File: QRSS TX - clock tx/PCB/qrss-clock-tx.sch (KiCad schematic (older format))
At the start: 1 part

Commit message: update QRSS TX schematic
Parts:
- removed U?: ATmega328PB-AU, Package_QFP:TQFP-32_7x7mm_P0.8mm, symbol MCU_Microchip_ATmega:ATmega328PB-AU
- added C1, C3, C4, C6, C7, C8: .1u, symbol Device:C
- added C10, C12: 30p, symbol Device:C
- added C11, C9: 10p, symbol Device:C
- added C2, C5: 100p, symbol Device:C
- added D1: POWER, symbol Device:LED
- added D2: VAR1, symbol Device:D_Capacitance
- added D3: VAR2, symbol Device:D_Capacitance
- added D4: STAT, symbol Device:LED
- added FB1: Ferrite_Bead, symbol Device:Ferrite_Bead
- added J1: PWR, symbol Connector:Conn_01x02_Male
- added J2: ICSP, symbol Connector:Conn_01x05_Male
- added J3: Conn_Coaxial, symbol Connector:Conn_Coaxial
- added Q1: MMBT3904, Package_TO_SOT_SMD:SOT-23, symbol Transistor_BJT:MMBT3904
- added R1, R2, R3, R6: 1K, symbol Device:R
- added R4: 100K, symbol Device:R
- added R5: 10K, symbol Device:R
- added U1, U2: LM78M05_TO252, Package_TO_SOT_SMD:TO-252-2, symbol Regulator_Linear:LM78M05_TO252
- added U3: 74HC04, symbol 74xx:74HC04
- added U4: ATtiny2313A-SU, Package_SO:SOIC-20W_7.5x12.8mm_P1.27mm, symbol MCU_Microchip_ATtiny:ATtiny2313A-SU
- added Y1: 10.14MHz, symbol Device:Crystal
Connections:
- new net: R6.1, U4.2 (PD0)
- new net: C12.1, U4.4 (PA1/XTAL2), Y1.1
- new net: C10.1, U4.5 (PA0/XTAL1), Y1.2
- new net: C11.2, C9.2, D2.1 (K), D3.1 (K), R4.1
- new net: C4.1, FB1.2, J1.2 (Pin_2)
- new net: D1.2 (A), R1.1
- new net: C3.1, R1.2, U2.3 (VO), U3.14 (VCC)
- new net: C7.2, R3.1, R4.2
- new net: Q1.1 (B), R2.1
- new net: D4.2 (A), R6.2
- new net: J3.1 (In), U3.10, U3.12, U3.2, U3.4, U3.6, U3.8
- new net: Q1.2 (E), R3.2
- new net CKOUT: U3.1, U3.11, U3.13, U3.3, U3.5, U3.9, U4.6 (PD2)
- new net GND: C1.2, C10.2, C11.1, C12.2, C2.2, C3.2, C4.2, C5.2, C6.2, C7.1, C8.2, C9.1, D1.1 (K), D2.2 (A), D3.2 (A), D4.1 (K), J1.1 (Pin_1), J2.1 (Pin_1), J3.2 (Ext), U1.2 (GND), U2.2 (GND), U3.7 (GND), U4.10 (GND)
- new net MCU5V: C1.1, C2.1, C8.1, Q1.3 (C), R5.2, U1.3 (VO), U4.20 (VCC)
- new net MISO: J2.4 (Pin_4), U4.18 (PB6)
- new net MOSI: J2.5 (Pin_5), U4.17 (PB5)
- new net RST: J2.2 (Pin_2), R5.1, U4.1 (PA2/~RESET)
- new net SCK: J2.3 (Pin_3), U4.19 (PB7)
- new net VCC: C5.1, C6.1, FB1.1, U1.1 (VI), U2.1 (VI)
- new net VarVLT: R2.2, U4.14 (PB2)
- no-connect marks 0 -> 9
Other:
- note added: "BUFFER AMPLIFIER"
- note added: "BUFFER POWER"
- note added: "FREQUENCY SHIFT KEYING"
- note added: "MCU POWER"
- note added: "OSCILLATOR/KEYER"
- note added: "Only 1 varactor is needed.\nBuild the board and test if\nXTAL1 and XTAL2 pins\nproduce different pulls"
- note added: "POWER INPUT"
- note added: "PROGRAMMER"
- note added: "customize values\nafter PWM freq\nis determined"
- note added: "https://github.com/swharden/AVR-projects/tree/master/QRSS%20TX%20-%20clock%20tx"

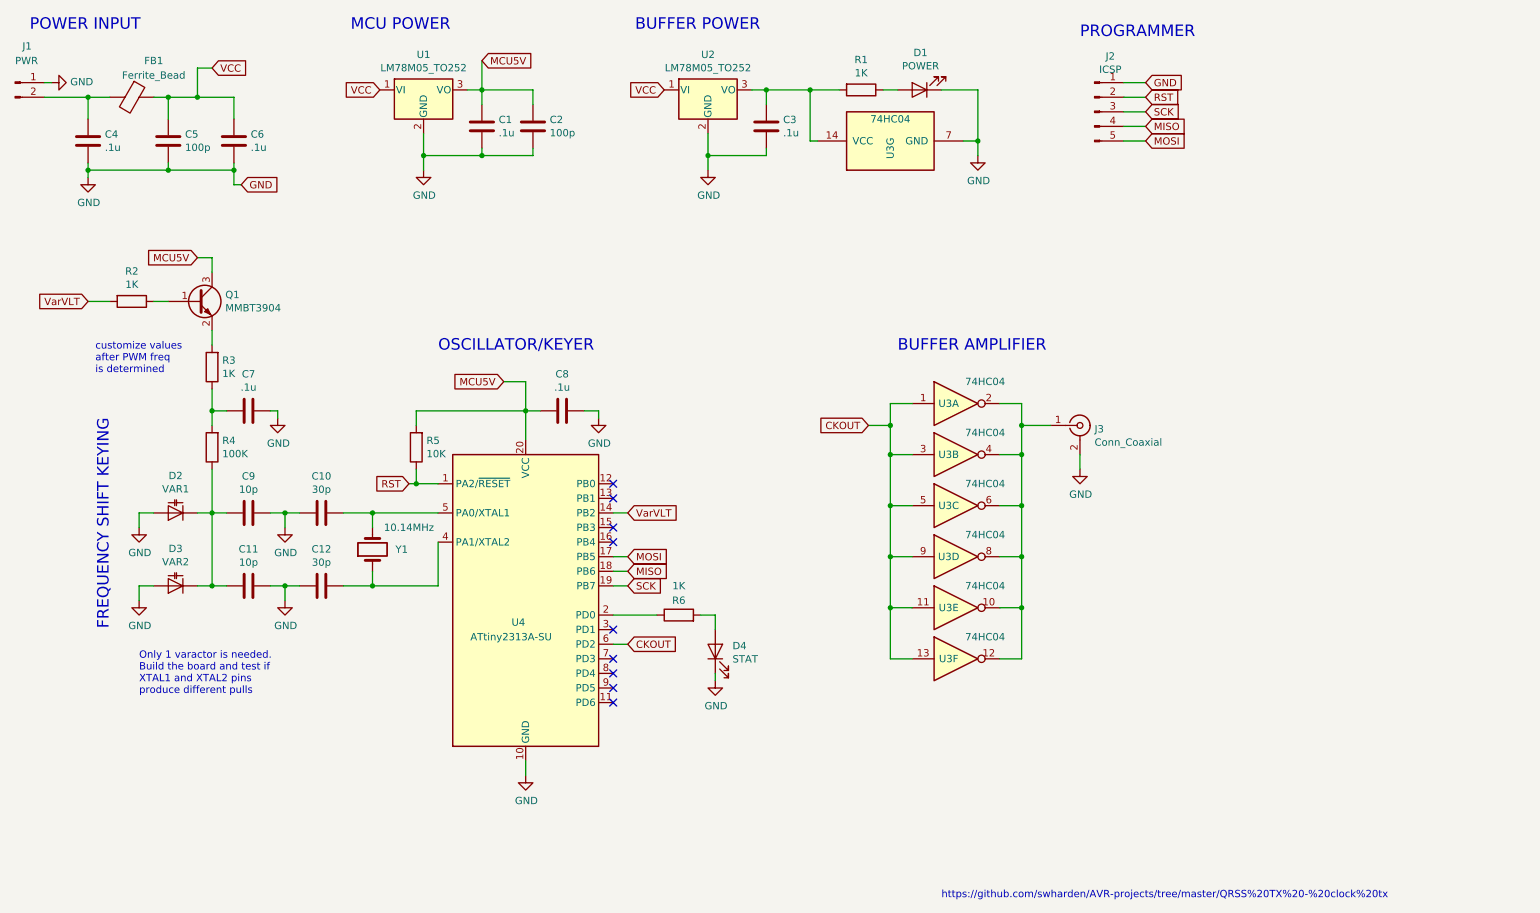
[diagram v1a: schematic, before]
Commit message: improve vFSK circuit
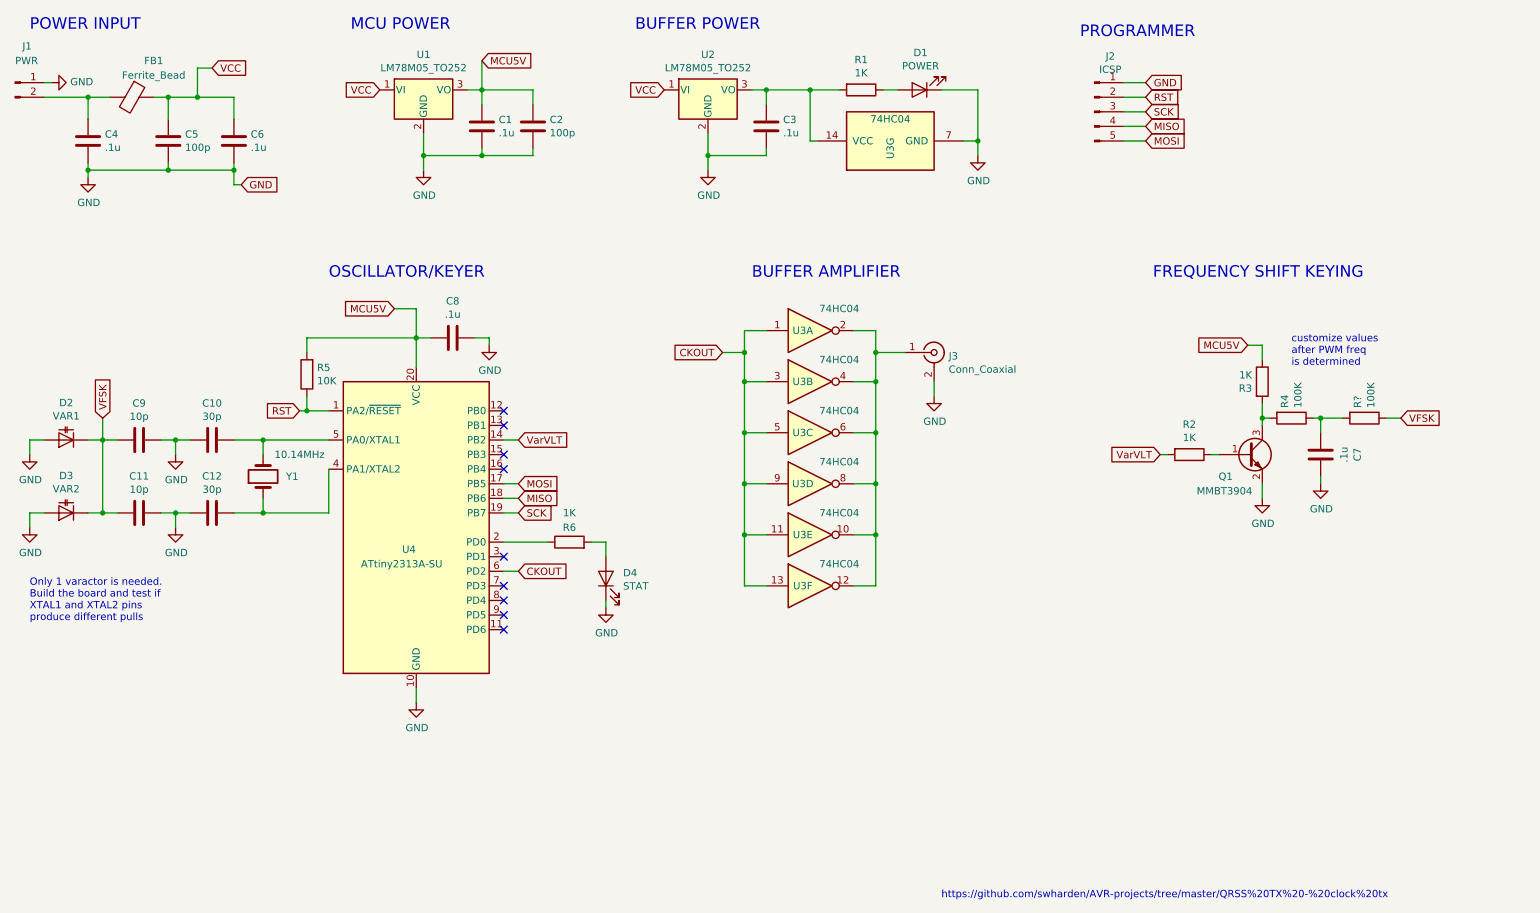
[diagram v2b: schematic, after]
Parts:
- added R?: 100K, symbol Device:R
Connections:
- net GND: now also Q1.2 (E)
- net MCU5V: now also R3.1; no longer Q1.3 (C)
- net VFSK: now reaches C11.2, C9.2, D2.1 (K), D3.1 (K)
- net VFSK: now also R?.1; no longer R4.1
- net at R3.2: now also Q1.3 (C), R4.2; no longer Q1.2 (E)
- new net: C7.2, R4.1, R?.2
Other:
- moved on the sheet: C10, C11, C12, C7, C8, C9, D2, D3, D4, J3, Q1, R2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

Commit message: Create CKOUT QRSS PCB (and 3D render)
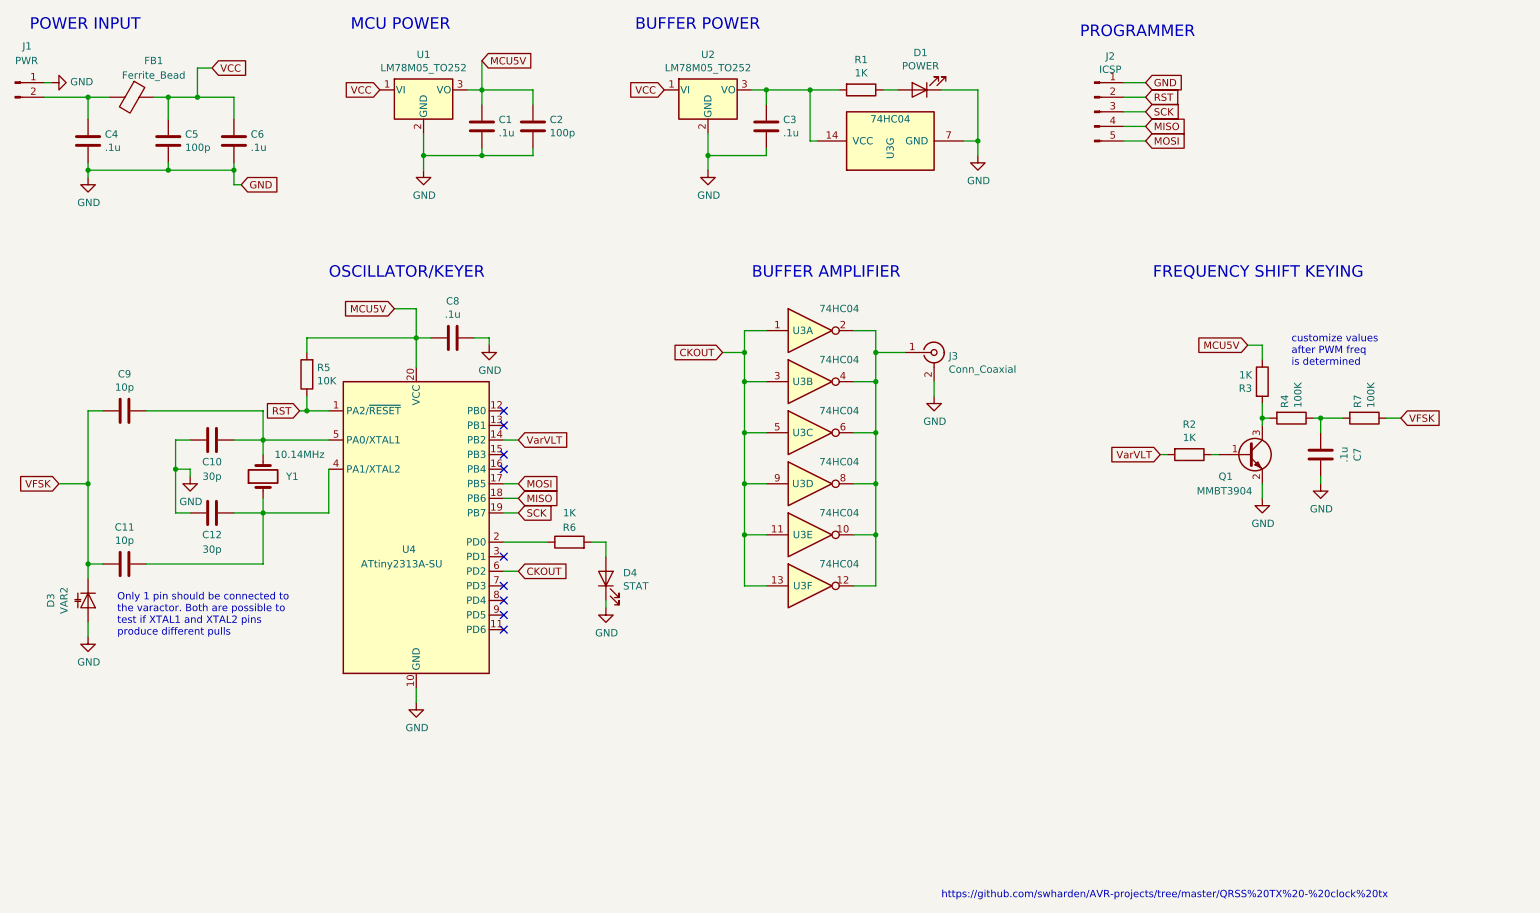
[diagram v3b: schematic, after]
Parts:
- removed D2: VAR1, symbol Device:D_Capacitance
- C1, C10, C11, C12, C2, C3, C4, C5, C6, C7, C8, C9: footprint (none) -> Capacitor_SMD:C_0805_2012Metric_Pad1.15x1.40mm_HandSolder
- D1, D4: footprint (none) -> LED_SMD:LED_0805_2012Metric_Pad1.15x1.40mm_HandSolder
- D3: footprint (none) -> Diode_SMD:D_0805_2012Metric_Pad1.15x1.40mm_HandSolder
- FB1, R1, R2, R3, R4, R5, R6: footprint (none) -> Resistor_SMD:R_0805_2012Metric_Pad1.15x1.40mm_HandSolder
- J1: footprint (none) -> Connector_PinHeader_2.54mm:PinHeader_1x02_P2.54mm_Vertical
- J2: footprint (none) -> Connector_PinHeader_2.54mm:PinHeader_1x05_P2.54mm_Vertical
- J3: footprint (none) -> Connector_Coaxial:SMA_Amphenol_132134-11_Vertical
- R7: renamed from R?; footprint (none) -> Resistor_SMD:R_0805_2012Metric_Pad1.15x1.40mm_HandSolder
- U3: footprint (none) -> Package_SO:SOIC-14_3.9x8.7mm_P1.27mm
- Y1: footprint (none) -> Crystal:Crystal_HC49-4H_Vertical
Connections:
- net GND: no longer C11.1, C9.1
- net at C12.1, U4.4 (PA1/XTAL2), Y1.1: now also C11.1
- net at C10.1, U4.5 (PA0/XTAL1), Y1.2: now also C9.1
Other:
- note added: "Only 1 pin should be connected to\nthe varactor. Both are possible to\ntest if XTAL1 and XTAL2 pins\nproduce different pulls"
- note removed: "Only 1 varactor is needed.\nBuild the board and test if\nXTAL1 and XTAL2 pins\nproduce different pulls"
- moved on the sheet: C11, C9, D3
